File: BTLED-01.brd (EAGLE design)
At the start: 85.1 x 58.4 mm, 17 parts

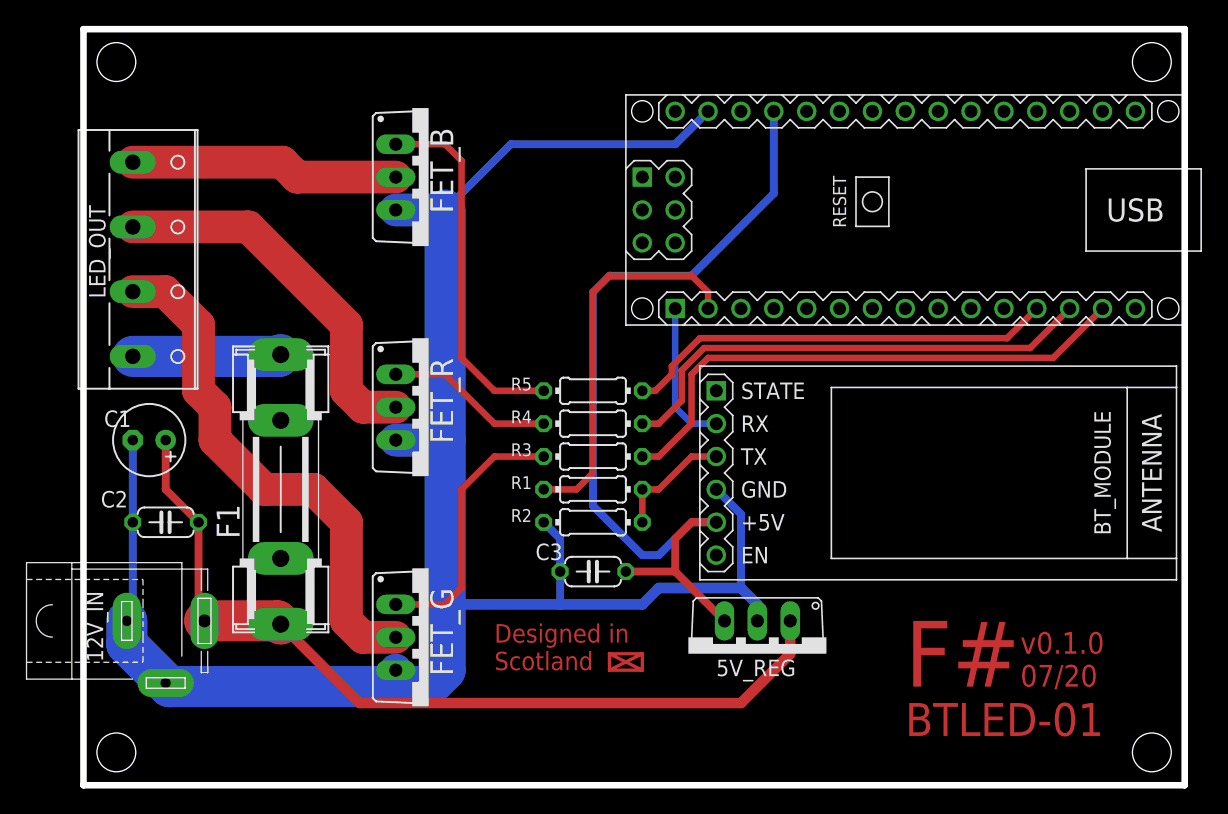
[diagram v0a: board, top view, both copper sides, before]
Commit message: fix: Replace fuse holder footprint
Replace 20mm fuse footprint with 22.5mm fuse holder.
Tweak some trace widths
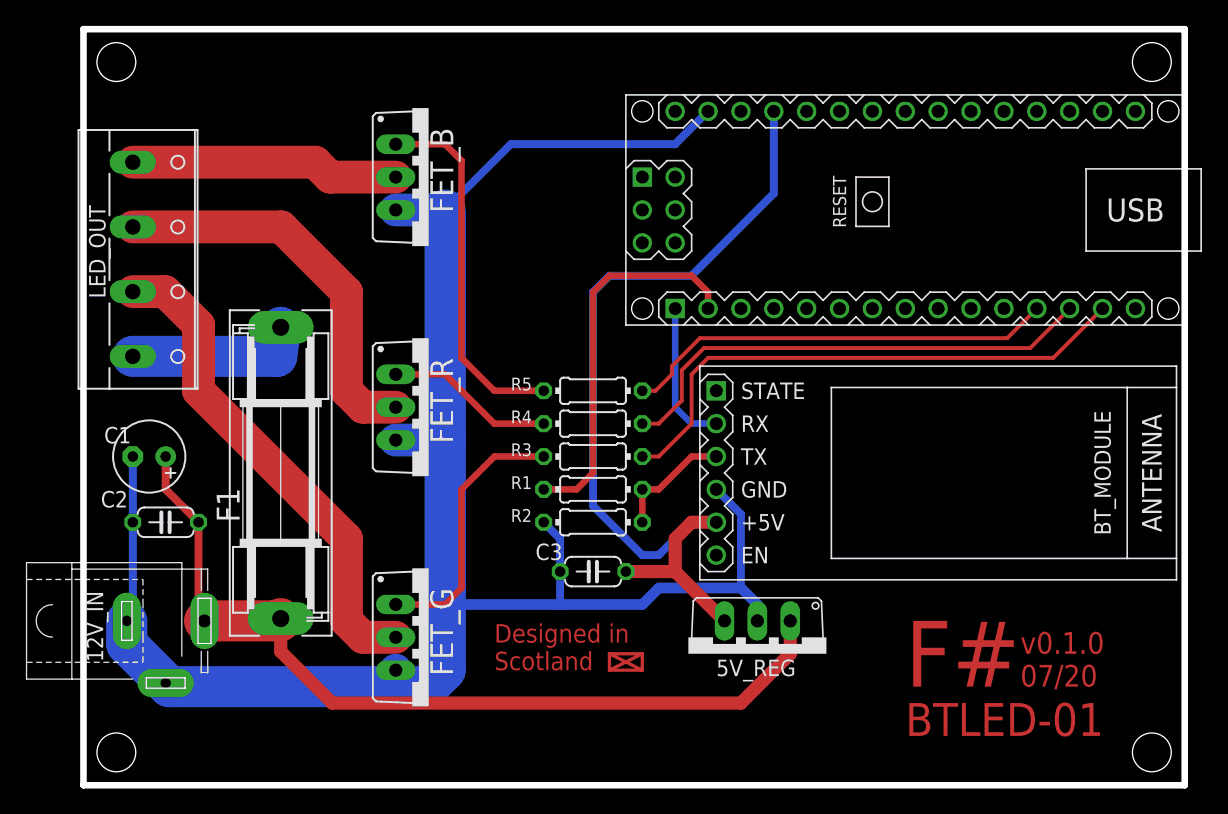
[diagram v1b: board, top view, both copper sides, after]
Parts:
- F1: value FUSESHK20L -> 13A; device fuse:SHK20L -> fuse:SH22,5
- moved F1 1.27 mm to (12.7, 52.1)
- moved C1 1.27 mm to (2.54, 53.3)
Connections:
- net 12V_IN: now also F1.1; no longer F1.1A
- net 12V_OUT: now also F1.2; no longer F1.2A
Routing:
- net G_DRAIN: track 40.3 -> 38.1 mm
- net 12V_OUT: track 11.5 -> 13.4 mm
- net R_DRAIN: track 29.1 -> 30.6 mm
- net GND: track 152.7 -> 151.5 mm

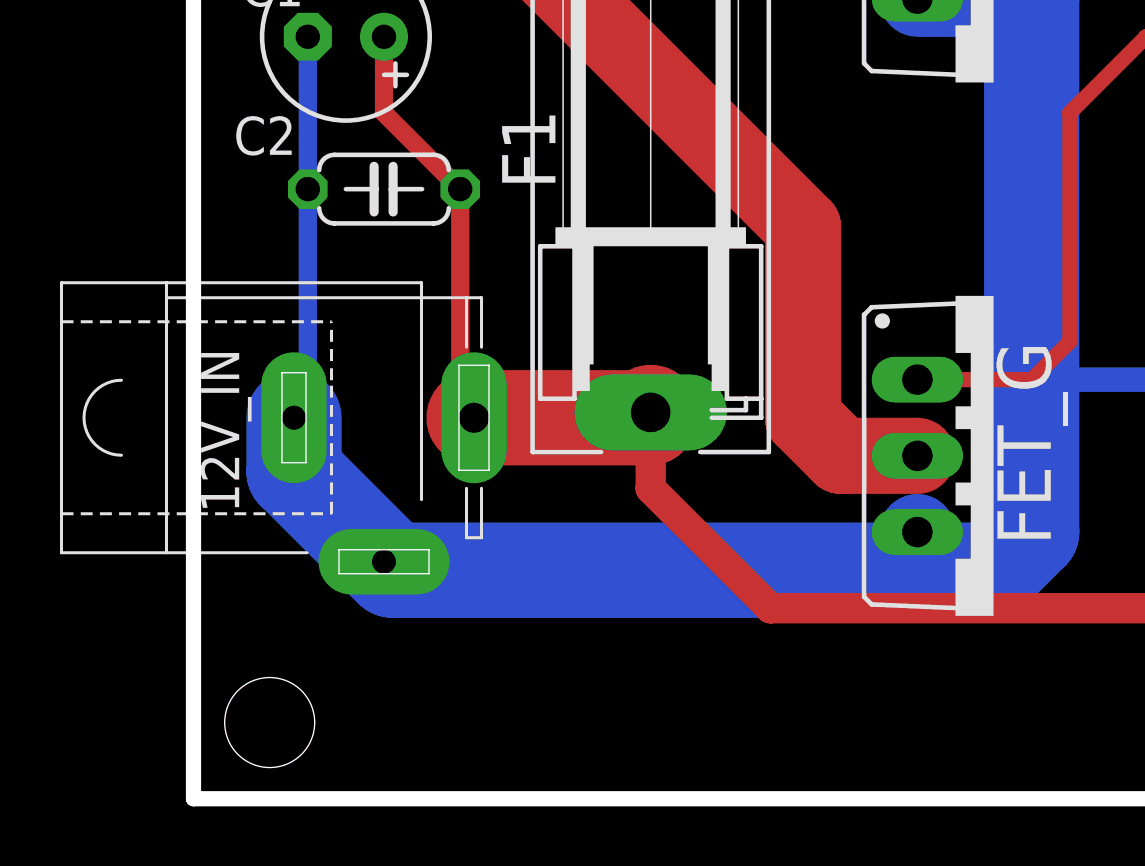
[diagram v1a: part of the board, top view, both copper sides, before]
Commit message: feat: Replaced DC input jack with Wago screw terminals
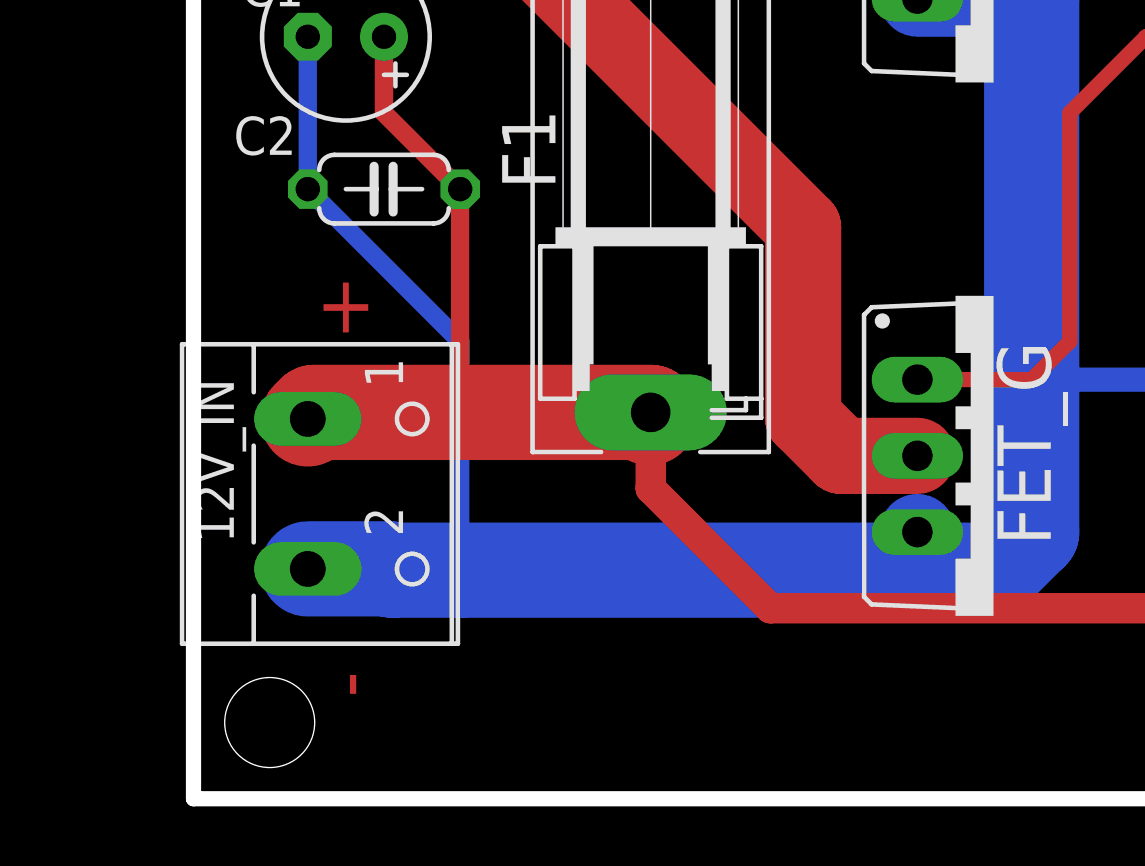
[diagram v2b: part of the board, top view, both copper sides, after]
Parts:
- 12V_IN: value 12V -> (none); device con-jack:SPC4078 -> con-wago-500:W237-102
- moved 12V_IN 2.84 mm to (2.54, 38.1), turned to 270 degrees
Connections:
- net 12V_IN: now also 12V_IN.1; no longer 12V_IN.3
- net GND: no longer 12V_IN.1
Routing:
- net 12V_IN: track 67.7 -> 72.7 mm
- net GND: track 151.5 -> 154.2 mm
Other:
- board text added: "+"
- board text added: "-"
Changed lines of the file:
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@@
 <text x="60.96" y="35.56" size="5.08" layer="1" font="vector" ratio="12" grouprefs="INFO_TEXT">F#</text>
 <text x="69.85" y="35.56" size="1.6764" layer="1" font="vector" ratio="10" grouprefs="INFO_TEXT">07/20</text>
+<text x="2.54" y="44.45" size="1.9304" layer="1" font="vector" align="center">+</text>
+<text x="2.54" y="31.75" size="1.9304" layer="1" font="vector" rot="R270" align="center">-</text>
 </plain>
 <attributes>
@@
 <attribute name="VALUE" x="54.61" y="45.72" size="1.27" layer="27" ratio="10" rot="R180"/>
 </element>
-<element name="12V_IN" library="con-jack" library_urn="urn:adsk.eagle:library:154" package="SPC4078" package3d_urn="urn:adsk.eagle:package:7494/1" value="12V" x="3.81" y="40.64" smashed="yes">
-<attribute name="MF" value="" x="35.56" y="0" size="1.778" layer="27" display="off"/>
-<attribute name="MPN" value="" x="35.56" y="0" size="1.778" layer="27" display="off"/>
-<attribute name="NAME" x="-1.016" y="37.465" size="1.27" layer="25" rot="R90"/>
-<attribute name="OC_FARNELL" value="unknown" x="35.56" y="0" size="1.778" layer="27" display="off"/>
-<attribute name="OC_NEWARK" value="unknown" x="35.56" y="0" size="1.778" layer="27" display="off"/>
-<attribute name="POPULARITY" value="3" x="35.56" y="0" size="1.778" layer="27" display="off"/>
-<attribute name="VALUE" x="-1.27" y="30.48" size="1.27" layer="27" rot="R90"/>
-</element>
 <element name="LED_OUT" library="con-wago-500" library_urn="urn:adsk.eagle:library:195" package="W237-4" package3d_urn="urn:adsk.eagle:package:10695/1" value="" x="2.54" y="68.58" smashed="yes" rot="R270">
 <attribute name="MF" value="" x="-35.56" y="21.59" size="1.778" layer="27" rot="R270" display="off"/>
@@
 <attribute name="SPICEPREFIX" value="R" x="36.83" y="58.42" size="1.778" layer="27" display="off"/>
 <attribute name="VALUE" x="35.2044" y="57.9374" size="0.9906" layer="27" ratio="10"/>
+</element>
+<element name="12V_IN" library="con-wago-500" library_urn="urn:adsk.eagle:library:195" package="W237-102" package3d_urn="urn:adsk.eagle:package:10688/1" value="" x="2.54" y="38.1" smashed="yes" rot="R270">
+<attribute name="MF" value="" x="2.54" y="38.1" size="1.778" layer="27" rot="R270" display="off"/>
+<attribute name="MPN" value="237-102" x="2.54" y="38.1" size="1.778" layer="27" rot="R270" display="off"/>
+<attribute name="NAME" x="-2.4638" y="41.9462" size="1.27" layer="25" ratio="10" rot="R270"/>
+<attribute name="OC_FARNELL" value="unknown" x="2.54" y="38.1" size="1.778" layer="27" rot="R270" display="off"/>
+<attribute name="OC_NEWARK" value="70K9898" x="2.54" y="38.1" size="1.778" layer="27" rot="R270" display="off"/>
+<attribute name="POPULARITY" value="32" x="2.54" y="38.1" size="1.778" layer="27" rot="R270" display="off"/>
+<attribute name="VALUE" x="-5.08" y="43.14" size="1.27" layer="27" ratio="10" rot="R270"/>
 </element>
 </elements>
@@
 </signal>
 <signal name="GND">
-<contactref element="12V_IN" pad="1"/>
 <contactref element="5V_REG" pad="2"/>
 <contactref element="C1" pad="-"/>
 <contactref element="C2" pad="2"/>
 <contactref element="C3" pad="2"/>
-<contactref element="12V_IN" pad="2"/>
 <contactref element="FET_B" pad="S"/>
 <contactref element="FET_R" pad="S"/>
 <contactref element="FET_G" pad="S"/>
-<wire x1="0.81" y1="40.64" x2="0.81" y2="38.84" width="3.175" layer="16"/>
-<wire x1="0.81" y1="38.84" x2="3.81" y2="35.84" width="3.175" layer="16"/>
-<wire x1="3.81" y1="35.84" x2="4.09" y2="35.56" width="3.175" layer="16"/>
 <wire x1="24.13" y1="35.56" x2="25.4" y2="36.83" width="3.175" layer="16"/>
 <wire x1="25.4" y1="54.61" x2="25.4" y2="41.91" width="3.175" layer="16"/>
 <wire x1="25.4" y1="41.91" x2="25.4" y2="36.83" width="3.175" layer="16"/>
-<wire x1="4.09" y1="35.56" x2="21.59" y2="35.56" width="3.175" layer="16"/>
+<wire x1="4.09" y1="35.56" x2="6.35" y2="35.56" width="3.175" layer="16"/>
+<wire x1="6.35" y1="35.56" x2="21.59" y2="35.56" width="3.175" layer="16"/>
 <wire x1="21.59" y1="35.56" x2="24.13" y2="35.56" width="3.175" layer="16"/>
 <wire x1="21.59" y1="54.61" x2="25.4" y2="54.61" width="2.54" layer="16"/>
 <wire x1="21.59" y1="36.83" x2="21.59" y2="35.56" width="2.54" layer="16"/>
-<wire x1="1.27" y1="41.1" x2="0.81" y2="40.64" width="0.6096" layer="1"/>
 <contactref element="BT_MODULE" pad="4"/>
 <contactref element="R2" pad="2"/>
@@
 <wire x1="43.18" y1="77.47" x2="30.48" y2="77.47" width="0.6096" layer="16"/>
 <wire x1="1.27" y1="53.34" x2="1.27" y2="48.26" width="0.6096" layer="16"/>
-<wire x1="1.27" y1="48.26" x2="1.27" y2="41.1" width="0.6096" layer="16"/>
-<wire x1="1.27" y1="41.1" x2="0.81" y2="40.64" width="0.6096" layer="16"/>
+<contactref element="12V_IN" pad="2"/>
+<wire x1="1.27" y1="35.6" x2="4.05" y2="35.6" width="3.175" layer="16"/>
+<wire x1="4.05" y1="35.6" x2="4.09" y2="35.56" width="3.175" layer="16"/>
+<wire x1="1.27" y1="48.26" x2="6.35" y2="43.18" width="0.6096" layer="16"/>
+<wire x1="6.35" y1="43.18" x2="6.35" y2="35.56" width="0.6096" layer="16"/>
 </signal>
 <signal name="12V_OUT">
@@
 <signal name="12V_IN">
 <contactref element="F1" pad="1"/>
-<contactref element="12V_IN" pad="3"/>
 <contactref element="C1" pad="+"/>
 <contactref element="C2" pad="1"/>
@@
 <wire x1="3.81" y1="50.8" x2="6.35" y2="48.26" width="0.6096" layer="1"/>
 <wire x1="6.35" y1="48.26" x2="6.35" y2="41.1" width="0.6096" layer="1"/>
-<wire x1="6.35" y1="41.1" x2="6.81" y2="40.64" width="0.6096" layer="1"/>
 <wire x1="52.07" y1="40.64" x2="52.07" y2="38.1" width="1.016" layer="1"/>
 <wire x1="12.7" y1="40.8178" x2="12.7" y2="38.2778" width="1.016" layer="1"/>
@@
 <wire x1="48.26" y1="34.29" x2="52.07" y2="38.1" width="1.016" layer="1"/>
 <wire x1="12.7" y1="40.8178" x2="12.65865" y2="40.64" width="3.175" layer="1"/>
-<wire x1="12.65865" y1="40.64" x2="6.81" y2="40.64" width="3.175" layer="1"/>
+<contactref element="12V_IN" pad="1"/>
+<wire x1="12.7" y1="40.8178" x2="1.4878" y2="40.8178" width="3.175" layer="1"/>
+<wire x1="1.4878" y1="40.8178" x2="1.27" y2="40.6" width="3.175" layer="1"/>
+<wire x1="1.27" y1="40.6" x2="6.35" y2="41.1" width="0" layer="19" extent="1-1"/>
 </signal>
 <signal name="G_DRAIN">
